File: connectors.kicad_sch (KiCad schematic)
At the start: 9 parts, among them J2 PANEL1, J3 PANEL2, J4 PANEL3, J5 PANEL4, J6 MTQZ

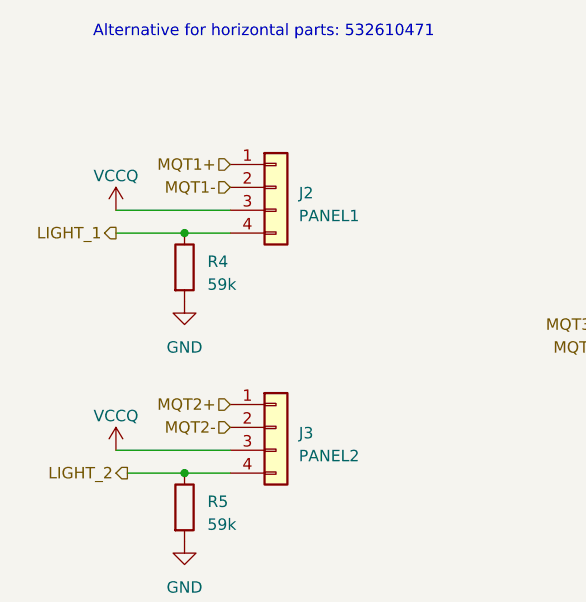
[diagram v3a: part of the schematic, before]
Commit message: Create PCB layout and routing
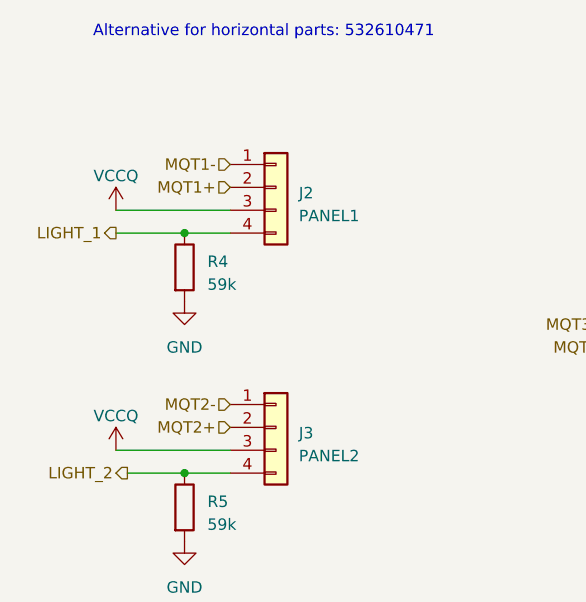
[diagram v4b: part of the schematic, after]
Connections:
- net MQT1+: now also J2.2 (Pin_2); no longer J2.1 (Pin_1)
- net MQT1-: now also J2.1 (Pin_1); no longer J2.2 (Pin_2)
- net MQT2+: now also J3.2 (Pin_2); no longer J3.1 (Pin_1)
- net MQT2-: now also J3.1 (Pin_1); no longer J3.2 (Pin_2)
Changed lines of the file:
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@@
     (effects (font (size 1.27 1.27)) (justify right))
   )
-  (hierarchical_label "MQT1+" (shape input) (at 121.92 55.88 180) (fields_autoplaced)
+  (hierarchical_label "MQT1-" (shape input) (at 121.92 55.88 180) (fields_autoplaced)
     (effects (font (size 1.27 1.27)) (justify right))
   )
-  (hierarchical_label "MQT2+" (shape input) (at 121.92 82.55 180) (fields_autoplaced)
+  (hierarchical_label "MQT2-" (shape input) (at 121.92 82.55 180) (fields_autoplaced)
     (effects (font (size 1.27 1.27)) (justify right))
   )
@@
     (effects (font (size 1.27 1.27)) (justify right))
   )
-  (hierarchical_label "MQT2-" (shape input) (at 121.92 85.09 180) (fields_autoplaced)
+  (hierarchical_label "MQT2+" (shape input) (at 121.92 85.09 180) (fields_autoplaced)
     (effects (font (size 1.27 1.27)) (justify right))
   )
-  (hierarchical_label "MQT1-" (shape input) (at 121.92 58.42 180) (fields_autoplaced)
+  (hierarchical_label "MQT1+" (shape input) (at 121.92 58.42 180) (fields_autoplaced)
     (effects (font (size 1.27 1.27)) (justify right))
   )

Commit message: Add files via upload
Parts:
- J6: footprint Connector_Molex:Molex_PicoBlade_53398-0371_1x03-1MP_P1.25mm_Vertical -> SQT-102-03-F-S:SAMTEC_SQT-102-03-F-S; symbol Connector_Generic:Conn_01x03 -> SQT-102-03-F-S:SQT-102-03-F-S; Availability (none) -> In Stock; Check_prices (none) -> https://www.snapeda.com/parts/SQT-102-03-F-S/Samtec/view-pa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; MANUFACTURER (none) -> SAMTEC; MF (none) -> Samtec Inc.; MP (none) -> SQT-102-03-F-S; Package (none) -> None; Price (none) -> None; Purchase-URL (none) -> https://www.snapeda.com/api/url_track_click_mouser/?unipart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; SnapEDA_Link (none) -> https://www.snapeda.com/parts/SQT-102-03-F-S/Samtec/view-pa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
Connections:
- net MQT3+: now also J6.01; no longer J6.2 (Pin_2)
- net MQT3-: now also J6.02; no longer J6.3 (Pin_3)
- no-connect marks 1 -> 0
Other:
- note added: "2-pin connector"
- note removed: "3-pin connector to avoid incompatible connections"
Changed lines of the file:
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@@
   (junction (at 116.84 115.57) (diameter 0) (color 0 0 0 0)
   )
-  (no_connect (at 165.1 71.12))
   (wire (pts (xy 116.84 115.57) (xy 121.92 115.57))
     (stroke (width 0) (type default))
@@
     (effects (font (size 1.27 1.27)) (justify left bottom))
   )
-  (text "3-pin connector to avoid incompatible connections" (at 180.34 74.93 0)
+  (text "2-pin connector " (at 182.88 69.85 0)
     (effects (font (size 1.27 1.27)) (justify left bottom))
   )
@@
     )
   )
-  (symbol (lib_id "Connector_Generic:Conn_01x03") (at 170.18 73.66 0) (unit 1)
+  (symbol (lib_id "SQT-102-03-F-S:SQT-102-03-F-S") (at 175.26 76.2 0) (unit 1)
     (in_bom yes) (on_board yes) (dnp no) (fields_autoplaced)
-    (property "Reference" "J6" (at 172.72 73.025 0)
+    (property "Reference" "J6" (at 181.61 73.66 0)
       (effects (font (size 1.27 1.27)) (justify left))
     )
-    (property "Value" "MTQZ" (at 172.72 75.565 0)
+    (property "Value" "MTQZ" (at 181.61 76.2 0)
       (effects (font (size 1.27 1.27)) (justify left))
     )
-    (property "Footprint" "Connector_Molex:Molex_PicoBlade_53398-0371_1x03-1MP_P1.25mm_Vertical" (at 170.18 73.66 0)
+    (property "Footprint" "SQT-102-03-F-S:SAMTEC_SQT-102-03-F-S" (at 175.26 76.2 0)
+      (effects (font (size 1.27 1.27)) (justify bottom) hide)
+    )
+    (property "Datasheet" "https://www.molex.com/en-us/products/part-detail/533980371?display=pdf" (at 175.26 76.2 0)
       (effects (font (size 1.27 1.27)) hide)
     )
-    (property "Datasheet" "https://www.molex.com/en-us/products/part-detail/533980371?display=pdf" (at 170.18 73.66 0)
+    (property "MPN" "533980371" (at 175.26 76.2 0)
       (effects (font (size 1.27 1.27)) hide)
     )
-    (property "MPN" "533980371" (at 170.18 73.66 0)
-      (effects (font (size 1.27 1.27)) hide)
+    (property "MF" "Samtec Inc." (at 175.26 76.2 0)
+      (effects (font (size 1.27 1.27)) (justify bottom) hide)
     )
-    (pin "1")
-    (pin "2")
-    (pin "3")
+    (property "Description" "\nSQT Series 2.00 mm FleXYZ™ Cost-effective Tiger Buy™ Square Tail Socket Strip\n" (at 175.26 76.2 0)
+      (effects (font (size 1.27 1.27)) (justify bottom) hide)
+    )
+    (property "Package" "None" (at 175.26 76.2 0)
+      (effects (font (size 1.27 1.27)) (justify bottom) hide)
+    )
+    (property "Price" "None" (at 175.26 76.2 0)
+      (effects (font (size 1.27 1.27)) (justify bottom) hide)
+    )
+    (property "Check_prices" "https://www.snapeda.com/parts/SQT-102-03-F-S/Samtec/view-part/?ref=eda" (at 175.26 76.2 0)
+      (effects (font (size 1.27 1.27)) (justify bottom) hide)
+    )
+    (property "SnapEDA_Link" "https://www.snapeda.com/parts/SQT-102-03-F-S/Samtec/view-part/?ref=snap" (at 175.26 76.2 0)
+      (effects (font (size 1.27 1.27)) (justify bottom) hide)
+    )
+    (property "MP" "SQT-102-03-F-S" (at 175.26 76.2 0)
+      (effects (font (size 1.27 1.27)) (justify bottom) hide)
+    )
+    (property "Purchase-URL" "https://www.snapeda.com/api/url_track_click_mouser/?unipart_id=4684469&manufacturer=Samtec Inc.&part_name=SQT-102-03-F-S&search_term=sqt-102-03-f-s" (at 175.26 76.2 0)
+      (effects (font (size 1.27 1.27)) (justify bottom) hide)
+    )
+    (property "Availability" "In Stock" (at 175.26 76.2 0)
+      (effects (font (size 1.27 1.27)) (justify bottom) hide)
+    )
+    (property "MANUFACTURER" "SAMTEC" (at 175.26 76.2 0)
+      (effects (font (size 1.27 1.27)) (justify bottom) hide)
+    )
+    (pin "01")
+    (pin "02")
     (instances
       (project "NEW_PCB_ADCS"

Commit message: Remove paste from connectors, relink GND mounting pins
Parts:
- J6: MPN 533980371 -> SQT-102-03-F-S
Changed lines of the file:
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@@
       (effects (font (size 1.27 1.27)) hide)
     )
-    (property "MPN" "533980371" (at 175.26 76.2 0)
+    (property "MPN" "SQT-102-03-F-S" (at 175.26 76.2 0)
       (effects (font (size 1.27 1.27)) hide)
     )

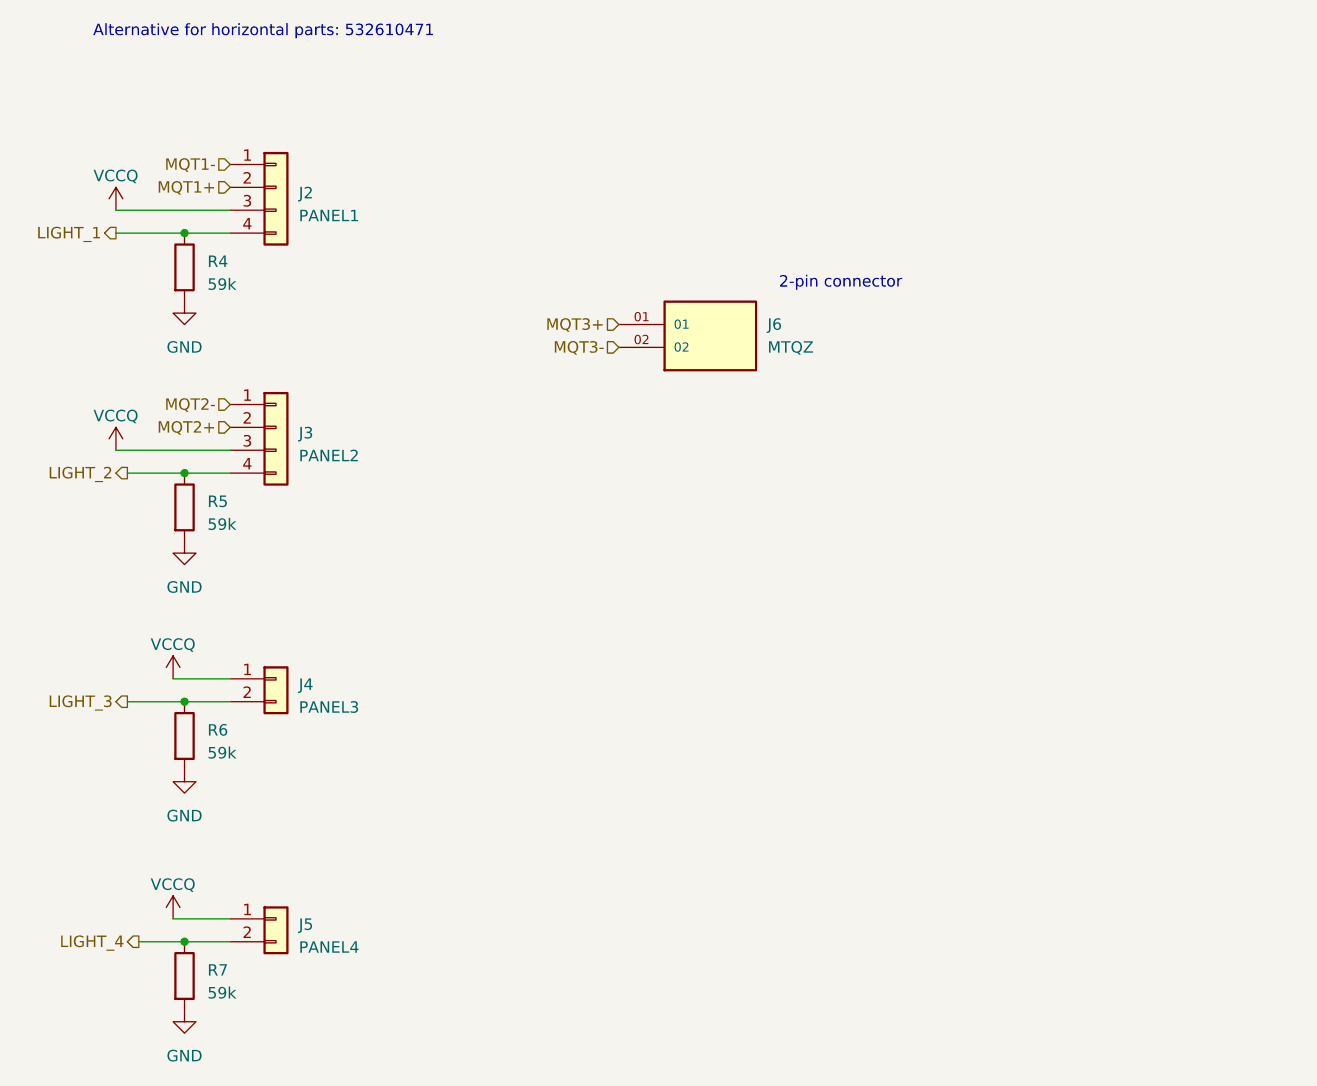
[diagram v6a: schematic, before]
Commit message: Use pogo pins; move diode to back
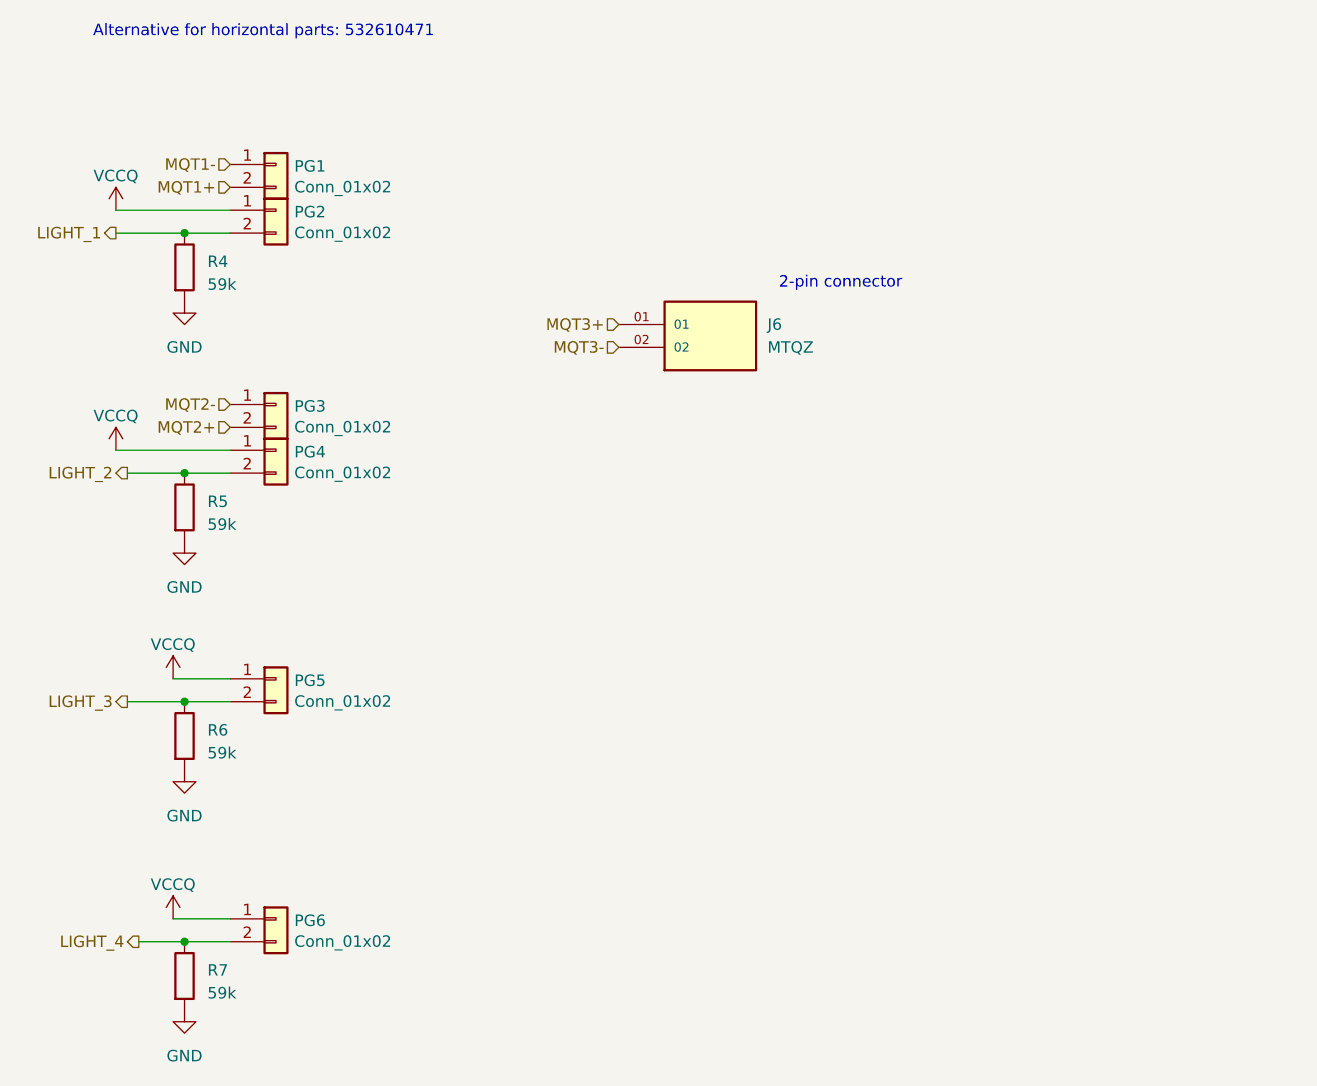
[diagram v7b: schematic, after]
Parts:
- removed J2: PANEL1, Connector_Molex:Molex_PicoBlade_53398-0471_1x04-1MP_P1.25mm_Vertical, symbol Connector_Generic:Conn_01x04
- removed J3: PANEL2, Connector_Molex:Molex_PicoBlade_53398-0471_1x04-1MP_P1.25mm_Vertical, symbol Connector_Generic:Conn_01x04
- removed J4: PANEL3, Connector_Molex:Molex_PicoBlade_53398-0271_1x02-1MP_P1.25mm_Vertical, symbol Connector_Generic:Conn_01x02
- removed J5: PANEL4, Connector_Molex:Molex_PicoBlade_53398-0271_1x02-1MP_P1.25mm_Vertical, symbol Connector_Generic:Conn_01x02
- added PG1, PG2, PG3, PG4, PG5, PG6: Conn_01x02, lsf-kicad-lib:MillMax_8290-22-002-20-001101_1x02_P2.54mm_Horizontal, symbol Connector_Generic:Conn_01x02
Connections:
- net LIGHT_1: now also PG2.2 (Pin_2)
- net LIGHT_2: now also PG4.2 (Pin_2)
- net LIGHT_3: now also PG5.2 (Pin_2)
- net LIGHT_4: now also PG6.2 (Pin_2)
- net MQT1+: now also PG1.2 (Pin_2)
- net MQT1-: now also PG1.1 (Pin_1)
- net MQT2+: now also PG3.2 (Pin_2)
- net MQT2-: now also PG3.1 (Pin_1)
- net VCCQ: now also PG2.1 (Pin_1), PG4.1 (Pin_1), PG5.1 (Pin_1), PG6.1 (Pin_1)

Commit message: Add ChipSat inhibit
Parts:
- added J2: MTQZ, Connector_JST:JST_SH_SM02B-SRSS-TB_1x02-1MP_P1.00mm_Horizontal, symbol SQT-102-03-F-S:SQT-102-03-F-S
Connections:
- net GND: now also J2.02
- new net INHIBIT: J2.01
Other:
- note added: "ChipSat control"
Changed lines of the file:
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@@
+    (effects (font (size 1.27 1.27)) (justify left bottom))
+  )
+  (text "ChipSat control" (at 182.88 87.63 0)
     (effects (font (size 1.27 1.27)) (justify left bottom))
   )
@@
   )
   (hierarchical_label "LIGHT_3" (shape output) (at 110.49 115.57 180) (fields_autoplaced)
+    (effects (font (size 1.27 1.27)) (justify right))
+  )
+  (hierarchical_label "INHIBIT" (shape input) (at 165.1 91.44 180) (fields_autoplaced)
     (effects (font (size 1.27 1.27)) (justify right))
   )
@@
     )
   )
+  (symbol (lib_id "power:GND") (at 165.1 93.98 0) (unit 1)
+    (in_bom yes) (on_board yes) (dnp no) (fields_autoplaced)
+    (property "Reference" "#PWR079" (at 165.1 100.33 0)
+      (effects (font (size 1.27 1.27)) hide)
+    )
+    (property "Value" "GND" (at 165.1 99.06 0)
+      (effects (font (size 1.27 1.27)))
+    )
+    (property "Footprint" "" (at 165.1 93.98 0)
+      (effects (font (size 1.27 1.27)) hide)
+    )
+    (property "Datasheet" "" (at 165.1 93.98 0)
+      (effects (font (size 1.27 1.27)) hide)
+    )
+    (pin "1")
+    (instances
+      (project "NEW_PCB_ADCS"
+        (path "/42c40d7d-71af-4ce9-bac9-d638f259c957/8584c500-e681-4774-8e2d-f320630e3d46"
+          (reference "#PWR079") (unit 1)
+        )
+      )
+    )
+  )
   (symbol (lib_id "Connector_Generic:Conn_01x02") (at 127 55.88 0) (unit 1)
     (in_bom yes) (on_board yes) (dnp no)
@@
         )
       )
+    )
+  )
+  (symbol (lib_id "SQT-102-03-F-S:SQT-102-03-F-S") (at 175.26 93.98 0) (unit 1)
+    (in_bom yes) (on_board yes) (dnp no) (fields_autoplaced)
+    (property "Reference" "J2" (at 181.61 91.44 0)
+      (effects (font (size 1.27 1.27)) (justify left))
+    )
+    (property "Value" "MTQZ" (at 181.61 93.98 0)
+      (effects (font (size 1.27 1.27)) (justify left))
+    )
+    (property "Footprint" "Connector_JST:JST_SH_SM02B-SRSS-TB_1x02-1MP_P1.00mm_Horizontal" (at 175.26 93.98 0)
+      (effects (font (size 1.27 1.27)) (justify bottom) hide)
+    )
+    (property "Datasheet" "" (at 175.26 93.98 0)
+      (effects (font (size 1.27 1.27)) hide)
+    )
+    (property "Part Number" "SM02B-SRSS-TB" (at 175.26 93.98 0)
+      (effects (font (size 1.27 1.27)) (justify bottom) hide)
+    )
+    (pin "01")
+    (pin "02")
+    (instances
+      (project "NEW_PCB_ADCS"
+        (path "/42c40d7d-71af-4ce9-bac9-d638f259c957/8584c500-e681-4774-8e2d-f320630e3d46"
+          (reference "J2") (unit 1)
+        )
+      )
